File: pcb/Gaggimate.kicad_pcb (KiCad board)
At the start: 2 copper layers, 85 x 82 mm, 85 parts, among them J1 USB_C_Receptacle, J2 Conn_01x02, J3 Conn_01x03, J4 Conn_01x04, J5 Conn_01x04, J6 Conn_01x10, J7 Conn_01x02, K1 Relay_SPDT, K2 Relay_SPDT, K3 Relay_SPDT, Q1 MMBT3904, Q2 MMBT3904, Q3 MMBT3904, SW1 SW_Push, SW2 SW_Push, U1 ESP32-S3-WROOM-1, U2 AMS1117-3.3, U3 LTV-817S, U4 LTV-817S, U5 LTV-817S, U6 MAX31855EASA

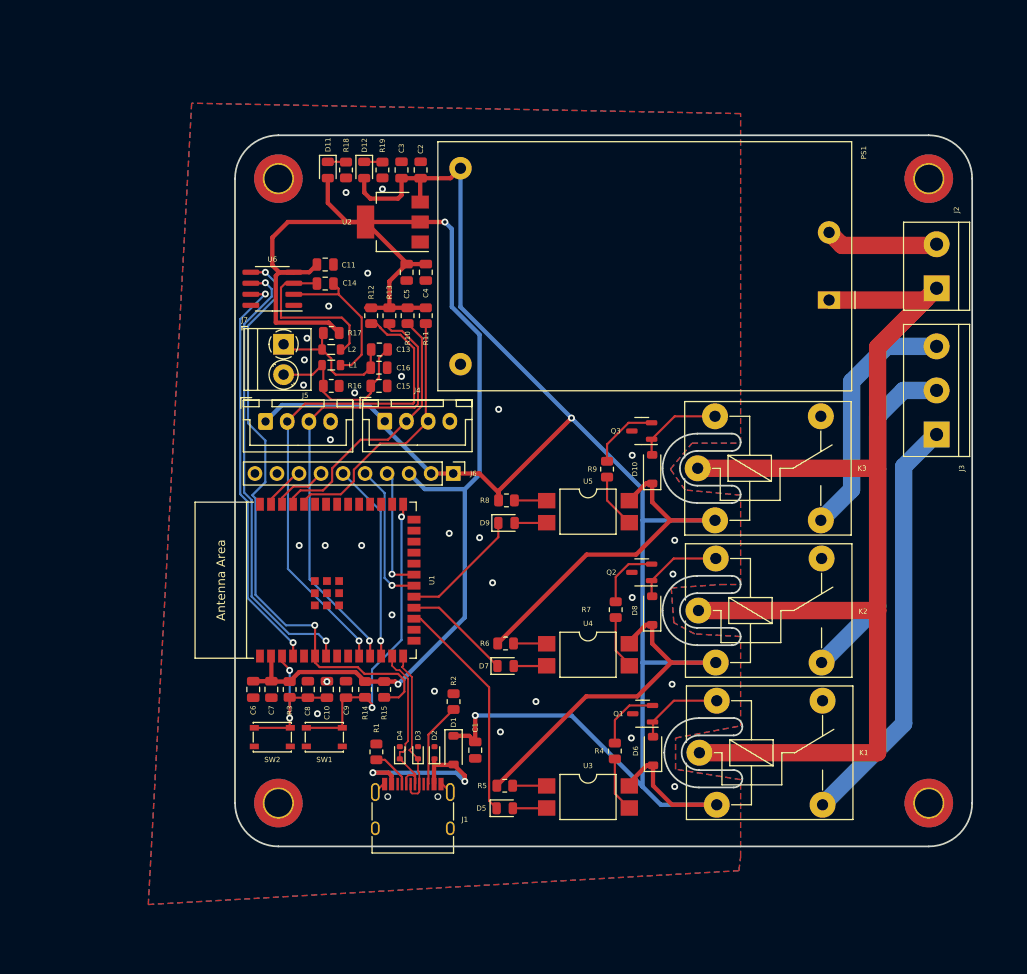
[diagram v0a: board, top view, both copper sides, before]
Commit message: feat: Shrink PCB by 16mm
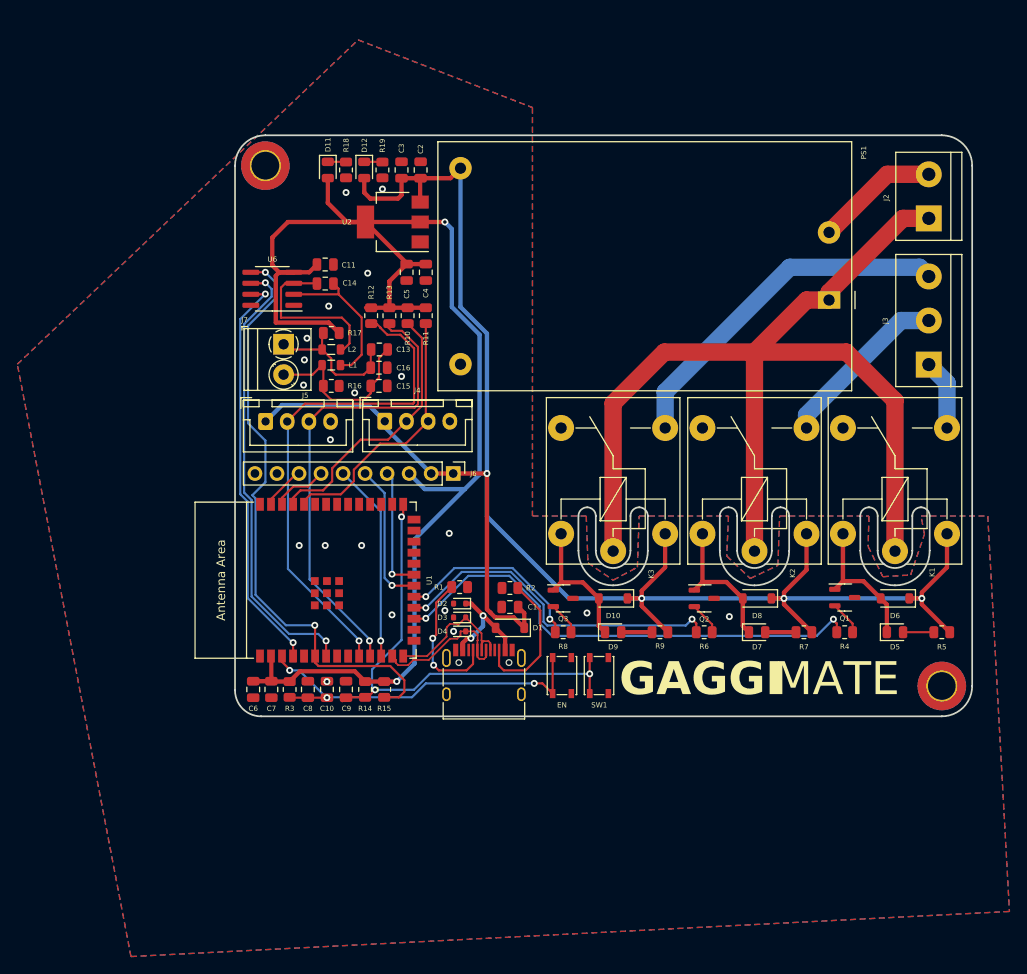
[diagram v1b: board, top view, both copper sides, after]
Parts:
- removed the H1 at (241.7, 31.1)
- removed the H1 at (166.7, 103.1)
- removed U3, U4, U5: LTV-817S, Package_DIP:SMDIP-4_W9.53mm
- Q1, Q2, Q3: value MMBT3904 -> MMBT2222
- R4: value 120R -> 1K
- R5: value 1K -> 150R
- R7, R9: value 120R -> 150R
- moved R5 53.4 mm to (243.2, 83.4), turned to 0 degrees
- moved D5 49.4 mm to (237.8, 83.4)
- moved EN 34.1 mm to (199.4, 88.4), turned to -90 degrees
- moved D6 33.0 mm to (237.8, 79.5), turned to 180 degrees
- moved SW1 32.5 mm to (203.7, 88.4), turned to -90 degrees
- moved K1 32.4 mm to (237.8, 74.0), turned to 90 degrees
- moved R4 29.8 mm to (232.0, 83.4), turned to 180 degrees
- moved D7 29.3 mm to (221.9, 83.4)
- moved Q1 26.9 mm to (232.0, 79.4), turned to 0 degrees
- moved R6 22.9 mm to (215.8, 83.4)
- moved R7 21.9 mm to (227.3, 83.4), turned to 0 degrees
- moved Q3 21.3 mm to (199.5, 79.5), turned to 0 degrees
- moved R1 21.3 mm to (187.6, 78.2), turned to 180 degrees
- moved R9 19.8 mm to (210.7, 83.4), turned to 0 degrees
- moved D9 17.6 mm to (205.3, 83.4)
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- renumbered SW2 to EN
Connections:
- D5 pad 1: /RELAY_PUMP -> Net-(D5-K)
- D6 pad 2: Net-(D6-A) -> Net-(D5-K)
- D7 pad 1: /RELAY_VALVE -> Net-(D7-K)
- D8 pad 2: Net-(D8-A) -> Net-(D7-K)
- D9 pad 1: /RELAY_GRINDER -> Net-(D10-A)
- H1 pad 1: (no net) -> GND
- K1 pad A2: Net-(D6-A) -> Net-(D5-K)
- K2 pad A2: Net-(D8-A) -> Net-(D7-K)
- Q1 pad 1: Net-(D6-A) -> Net-(D5-K)
- Q2 pad 1: Net-(D8-A) -> Net-(D7-K)
- R4 pad 2: Net-(R4-Pad2) -> /RELAY_PUMP
- R5 pad 1: Net-(R5-Pad1) -> Net-(D5-A)
- R6 pad 1: Net-(R6-Pad1) -> Net-(Q2-B)
- R6 pad 2: +5V -> /RELAY_VALVE
- R7 pad 1: Net-(Q2-B) -> Net-(D7-A)
- R7 pad 2: Net-(R7-Pad2) -> +5V
- R8 pad 1: Net-(R8-Pad1) -> Net-(Q3-B)
- R8 pad 2: +5V -> /RELAY_GRINDER
- R9 pad 1: Net-(Q3-B) -> Net-(D9-A)
- R9 pad 2: Net-(R9-Pad2) -> +5V
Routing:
- net +5V: track 292.6 -> 213.3 mm, vias 2 -> 4
- net /LINE_PUMP: track 48.1 -> 8.18 mm
- net /RELAY_PUMP: track 26.2 -> 57.1 mm, vias 0 -> 2
- net /RELAY_VALVE: track 12.4 -> 39.6 mm, vias 0 -> 2
- net /CHIP_PU: track 19.8 -> 43.6 mm, vias 2 -> 3
- net /BOOT: track 36.7 -> 57.3 mm, vias 2 -> 3
- net /LINE_VALVE: track 39.0 -> 20.1 mm
- net Net-(D7-K): track 0.00 -> 16.5 mm
- net Net-(D5-K): track 0.00 -> 16.2 mm
- net LINE: track 137.1 -> 121.6 mm
- net /LINE_GRINDER: track 28.9 -> 40.9 mm
- net Net-(J1-CC1): track 4.60 -> 16.7 mm, vias 0 -> 2
- net Net-(D8-A): track 10.3 -> 0.00 mm
- net Net-(D6-A): track 10.2 -> 0.00 mm
- net /VBUS: track 21.9 -> 13.0 mm
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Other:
- board size 85 x 82 mm -> 85 x 67 mm
- board text removed: "Control PCB v0.1"

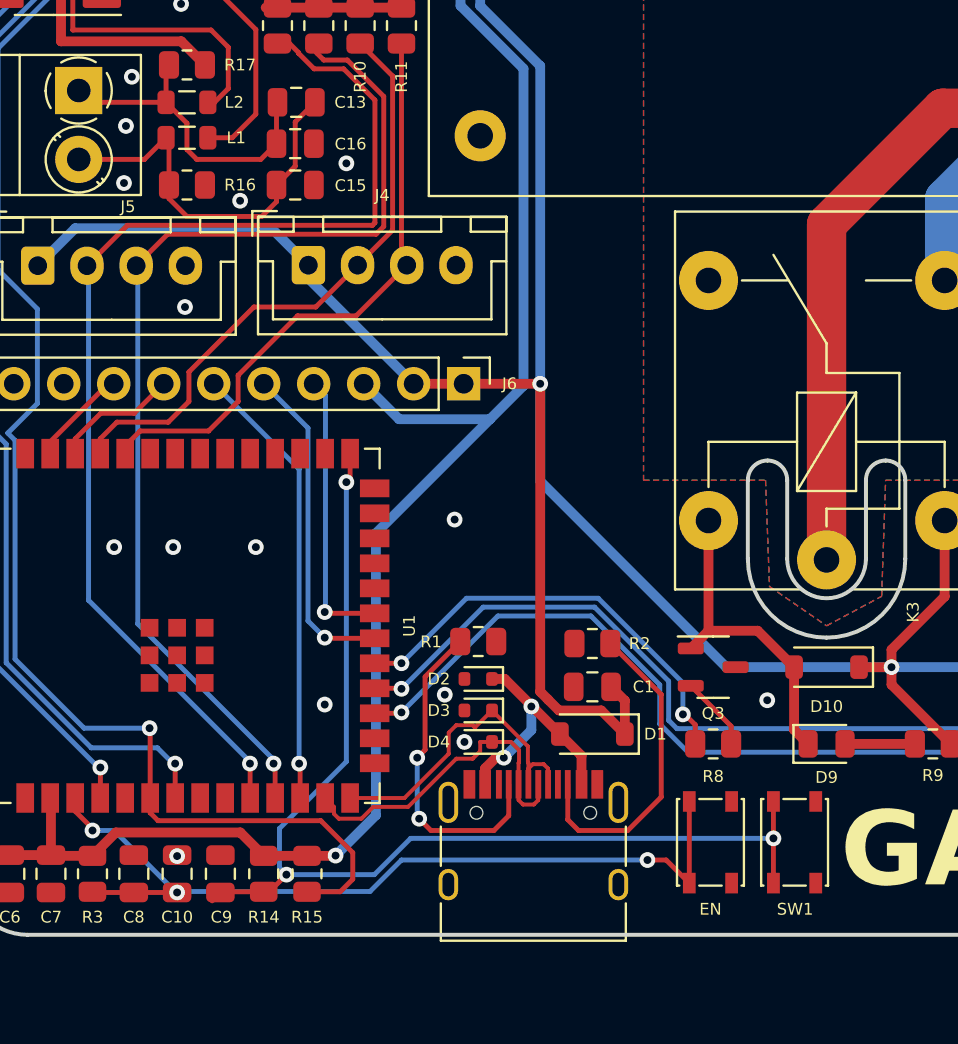
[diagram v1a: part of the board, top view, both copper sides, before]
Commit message: feat: Change USB routing on PCB
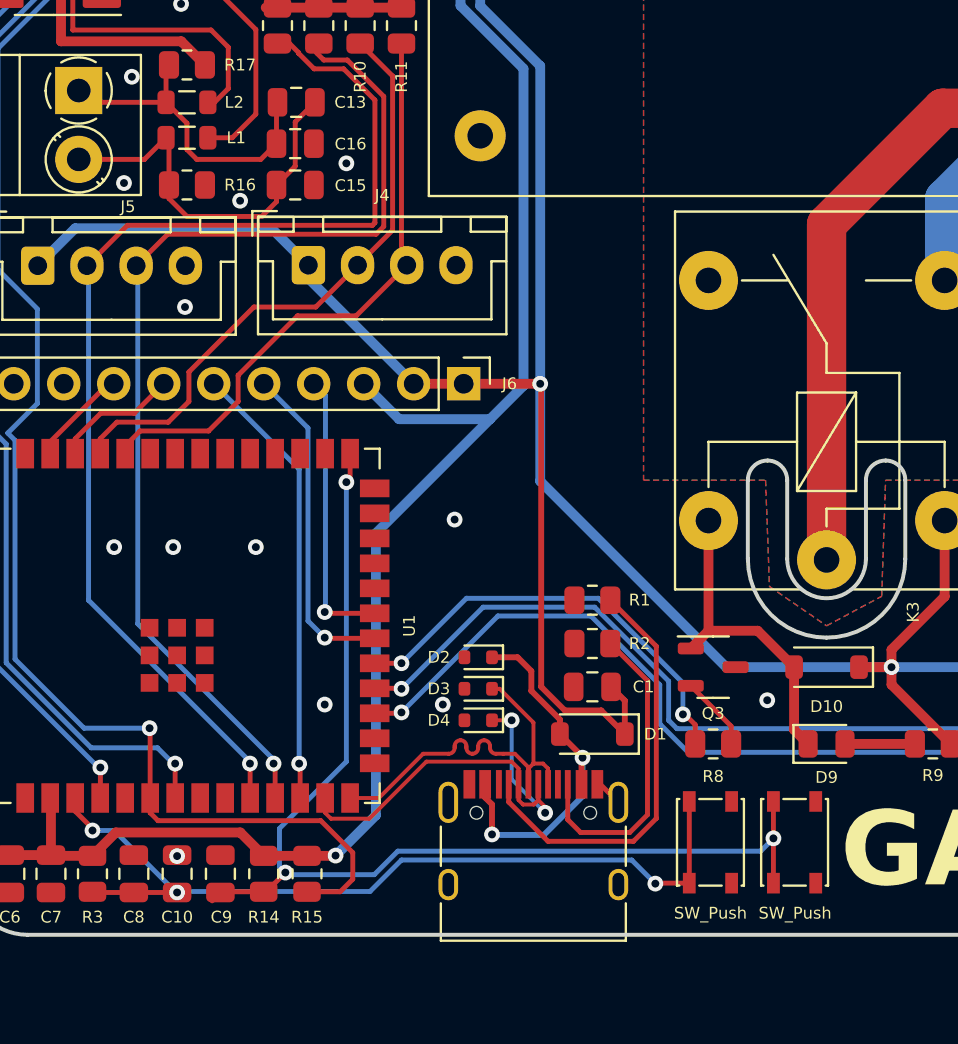
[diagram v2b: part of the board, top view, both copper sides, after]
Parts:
- moved R1 6.17 mm to (193.4, 76.1), turned to 0 degrees
- moved D3 1.10 mm to (187.6, 80.6)
- moved D2 1.10 mm to (187.6, 79.0)
- moved D4 1.10 mm to (187.6, 82.2)
- renumbered EN to SW2
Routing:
- net /VBUS: track 13.0 -> 19.3 mm
- net /USB_DN: track 17.1 -> 22.9 mm, vias 0 -> 2
- net Net-(J1-CC1): track 16.7 -> 21.8 mm, vias 2 -> 0
- net /USB_DP: track 17.7 -> 21.1 mm
- net GND: track 0.29 -> 1.74 mm, vias 20 -> 18

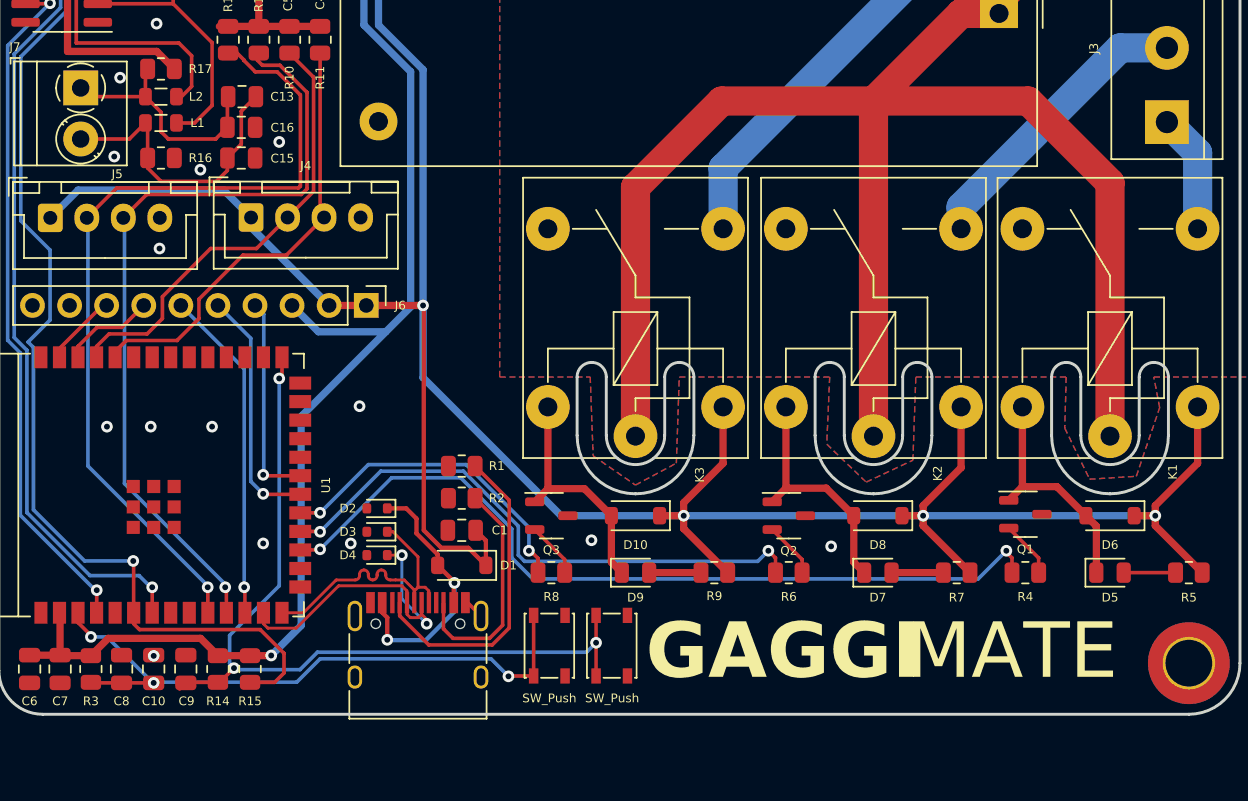
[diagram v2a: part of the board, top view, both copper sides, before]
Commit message: fix: Fix PCB buttons, traces
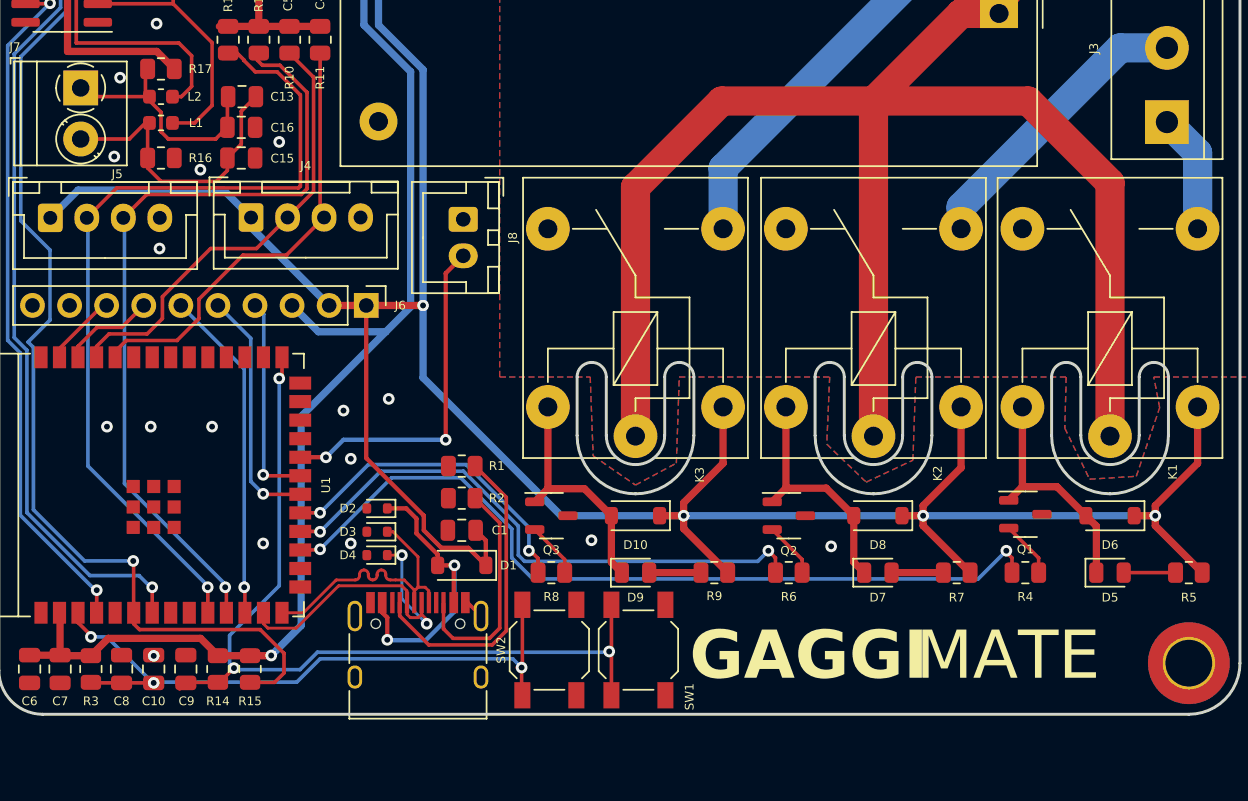
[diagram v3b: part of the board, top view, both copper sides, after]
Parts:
- added J8: Conn_01x02, Connector_JST:JST_XH_B2B-XH-A_1x02_P2.50mm_Vertical, F.Cu at (193.5, 59.2)
- L1, L2: footprint Inductor_SMD:L_0805_2012Metric -> Inductor_SMD:L_0603_1608Metric
- SW1, SW2: footprint Button_Switch_SMD:SW_SPST_PTS810 -> Button_Switch_SMD:SW_SPST_SKQG_WithStem
- moved SW1 1.85 mm to (205.5, 88.7)
- moved SW2 0.30 mm to (199.4, 88.7)
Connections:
- U1 pad 22: /GPIO14 -> /SSR
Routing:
- net /SSR: track 0.00 -> 23.7 mm, vias 0 -> 2
- net /BOOT: track 57.2 -> 60.3 mm
- net /VBUS: track 19.3 -> 21.1 mm
- net +5V: track 213.1 -> 214.7 mm
- net /CHIP_PU: track 43.6 -> 44.9 mm
- net GND: vias 18 -> 20

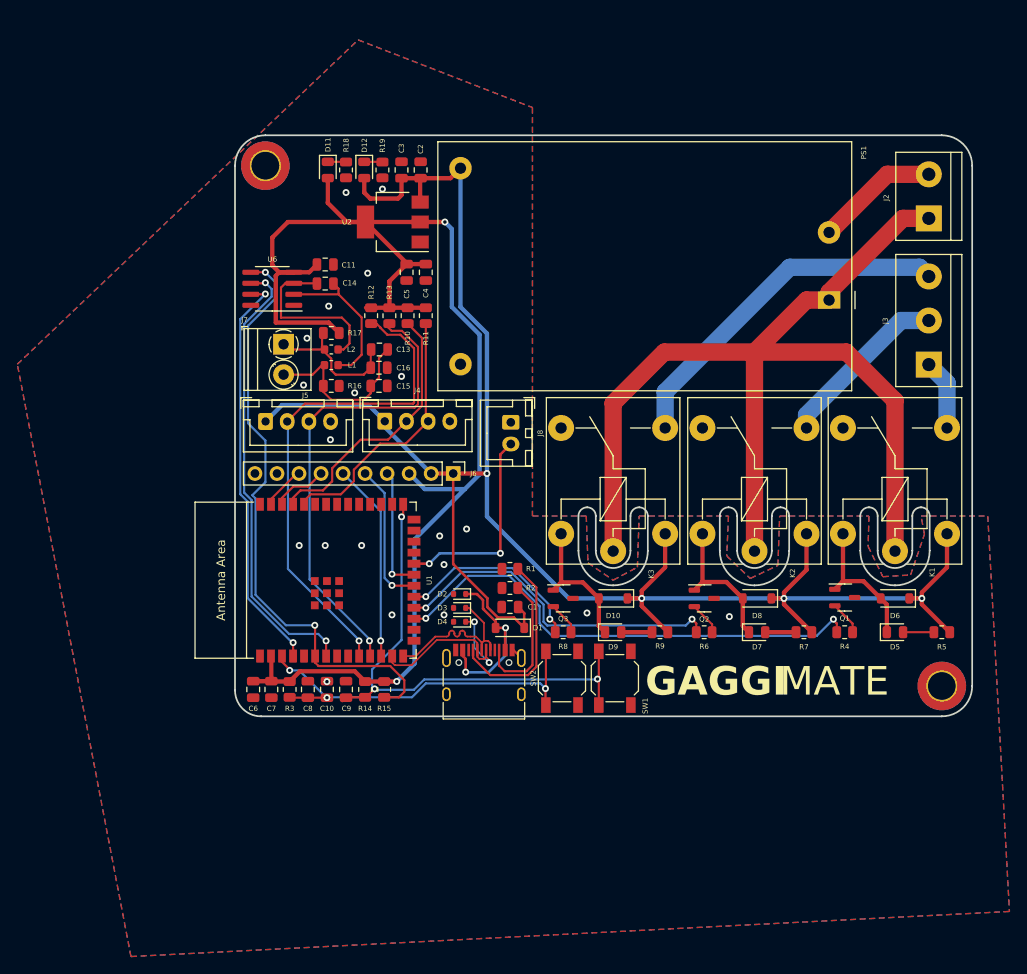
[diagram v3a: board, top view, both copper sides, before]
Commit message: feat: Add button connector to PCB, change pcbdraw
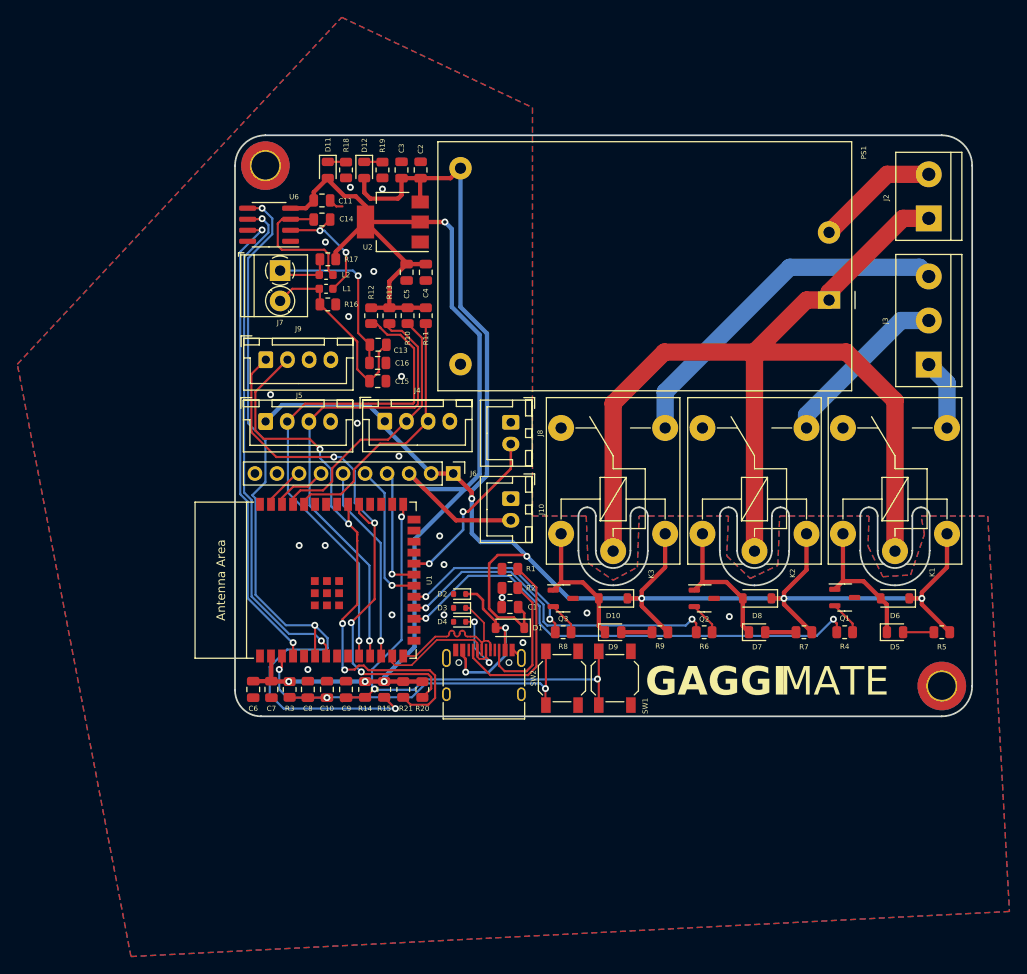
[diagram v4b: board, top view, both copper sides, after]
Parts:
- added J10: Conn_01x02, Connector_JST:JST_XH_B2B-XH-A_1x02_P2.50mm_Vertical, F.Cu at (193.5, 68.0)
- added J9: Conn_01x04, Connector_JST:JST_XH_B4B-XH-A_1x04_P2.50mm_Vertical, F.Cu at (165.2, 52.0)
- added R20: 10K, Resistor_SMD:R_0805_2012Metric, F.Cu at (183.3, 90.0)
- added R21: 10K, Resistor_SMD:R_0805_2012Metric, F.Cu at (181.1, 90.0)
- moved R16 9.41 mm to (172.4, 45.6)
- moved L1 8.82 mm to (172.2, 43.8)
- moved L2 8.62 mm to (172.2, 42.2)
- moved J7 8.51 mm to (166.9, 41.7)
- moved R17 8.51 mm to (172.4, 40.4)
- moved kibuzzard-671EE717 8.51 mm to (171.9, 45.2)
- moved kibuzzard-671EE722 8.41 mm to (172.0, 41.8)
- moved C11 7.40 mm to (171.7, 33.6)
- moved C14 7.40 mm to (171.7, 35.8)
- moved U6 7.40 mm to (165.6, 36.4)
- moved C13 0.57 mm to (178.2, 50.2)
- moved C15 0.57 mm to (178.2, 54.5)
- moved C16 0.57 mm to (178.2, 52.4)
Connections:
- U1 pad 23: unconnected-(U1-GPIO21-Pad23) -> /GPIO21
- U1 pad 24: unconnected-(U1-GPIO47/SPICLK_P/SUBSPICLK_P_DIFF-Pad24) -> /GPIO47
- U1 pad 25: unconnected-(U1-GPIO48/SPICLK_N/SUBSPICLK_N_DIFF-Pad25) -> /GPIO48
- U1 pad 31: unconnected-(U1-GPIO38/FSPIWP/SUBSPIWP-Pad31) -> /BTN_BREW
- U1 pad 32: unconnected-(U1-MTCK/GPIO39/CLK_OUT3/SUBSPICS1-Pad32) -> /BTN_STEAM
- U1 pad 33: unconnected-(U1-MTDO/GPIO40/CLK_OUT2-Pad33) -> /GPIO40
- U1 pad 34: unconnected-(U1-MTDI/GPIO41/CLK_OUT1-Pad34) -> /GPIO41
- U1 pad 35: unconnected-(U1-MTMS/GPIO42-Pad35) -> /GPIO42
- U1 pad 8: unconnected-(U1-GPIO15/U0RTS/ADC2_CH4/XTAL_32K_P-Pad8) -> /GPIO15
- U1 pad 9: unconnected-(U1-GPIO16/U0CTS/ADC2_CH5/XTAL_32K_N-Pad9) -> /GPIO16
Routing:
- net /BTN_STEAM: track 0.00 -> 66.5 mm, vias 0 -> 4
- net /BTN_BREW: track 0.00 -> 63.0 mm, vias 0 -> 4
- net /SPI_CLK: track 70.1 -> 92.7 mm, vias 2 -> 3
- net Net-(J7-Pin_1): track 17.0 -> 26.4 mm, vias 0 -> 1
- net +3.3V: track 160.7 -> 152.7 mm, vias 2 -> 4
- net /SPI_MISO: track 47.6 -> 54.8 mm
- net /MAX_CS: track 52.6 -> 59.2 mm
- net +5V: track 214.7 -> 210.6 mm, vias 4 -> 5
- net Net-(U6-T+): track 19.8 -> 15.8 mm
- net Net-(U6-T-): track 18.0 -> 14.1 mm, vias 0 -> 2
- net /SSR: track 23.7 -> 19.8 mm
- net /CHIP_PU: track 44.9 -> 48.2 mm
- net Net-(J7-Pin_2): track 19.9 -> 23.2 mm
- net GND: track 1.74 -> 3.57 mm
